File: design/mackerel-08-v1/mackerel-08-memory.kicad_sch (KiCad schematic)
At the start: 8 parts, among them U2 AS6C4008-55PCN, U3 SST39SF040, U4 AS6C4008-55PCN, U5 AS6C4008-55PCN, U6 AS6C4008-55PCN, U7 AS6C4008-55PCN, U8 AS6C4008-55PCN, U9 AS6C4008-55PCN

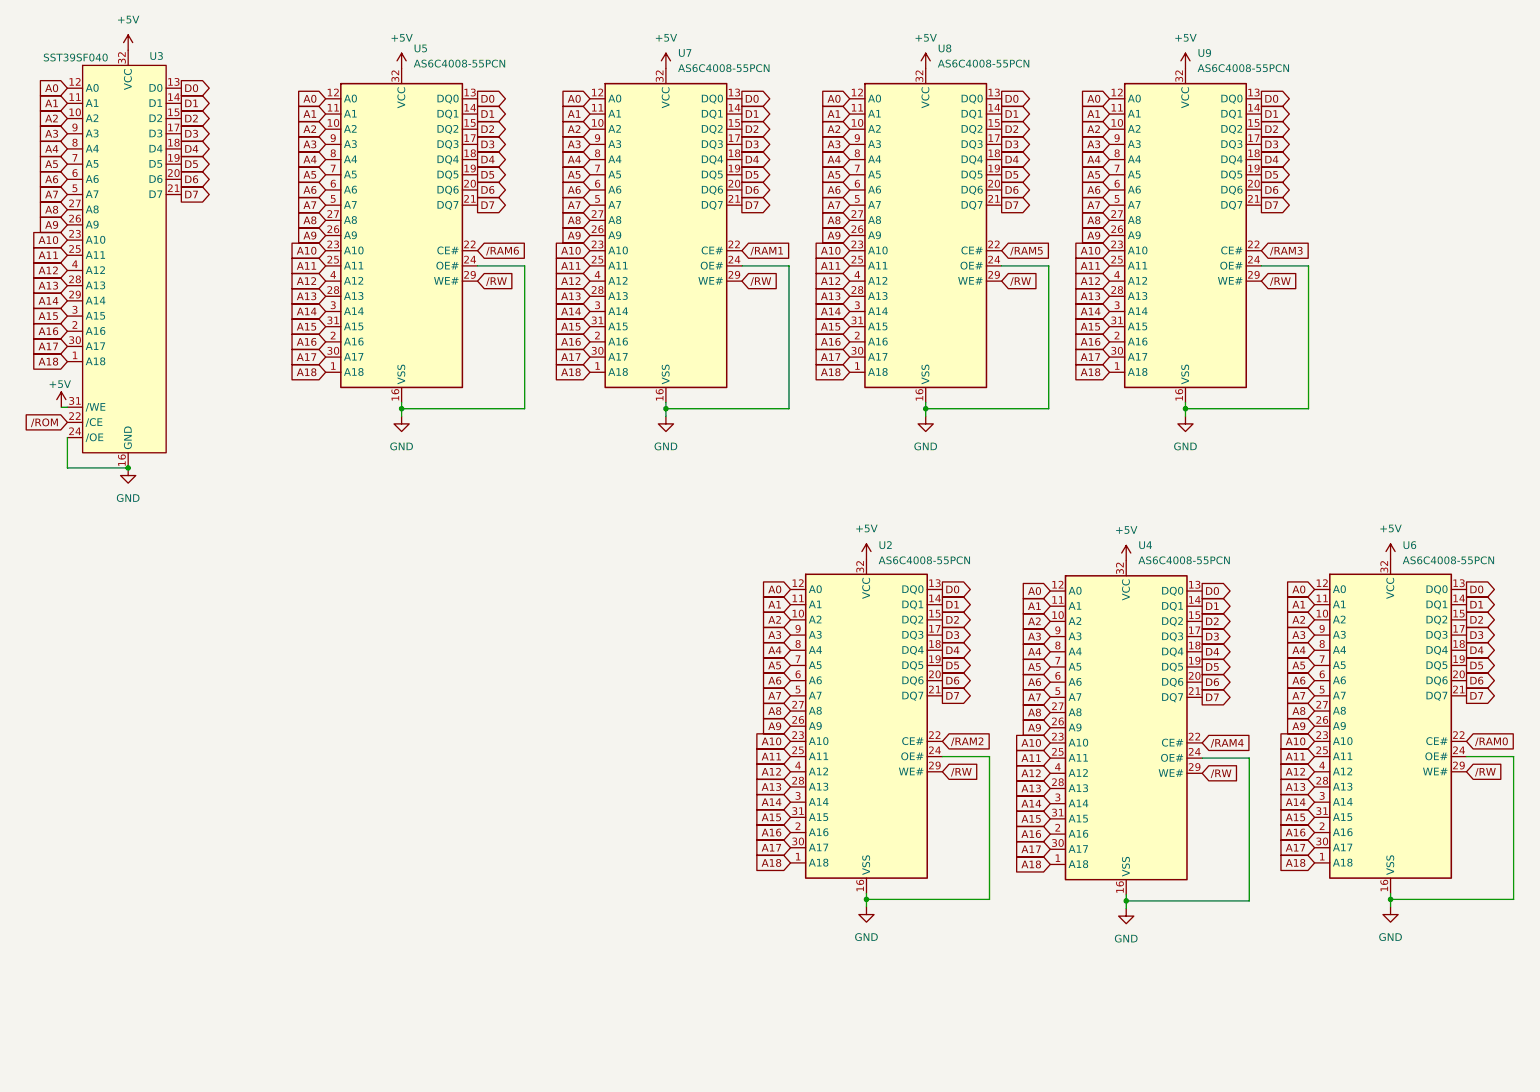
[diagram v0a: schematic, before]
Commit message: Clean up the schematic, ready for final routing
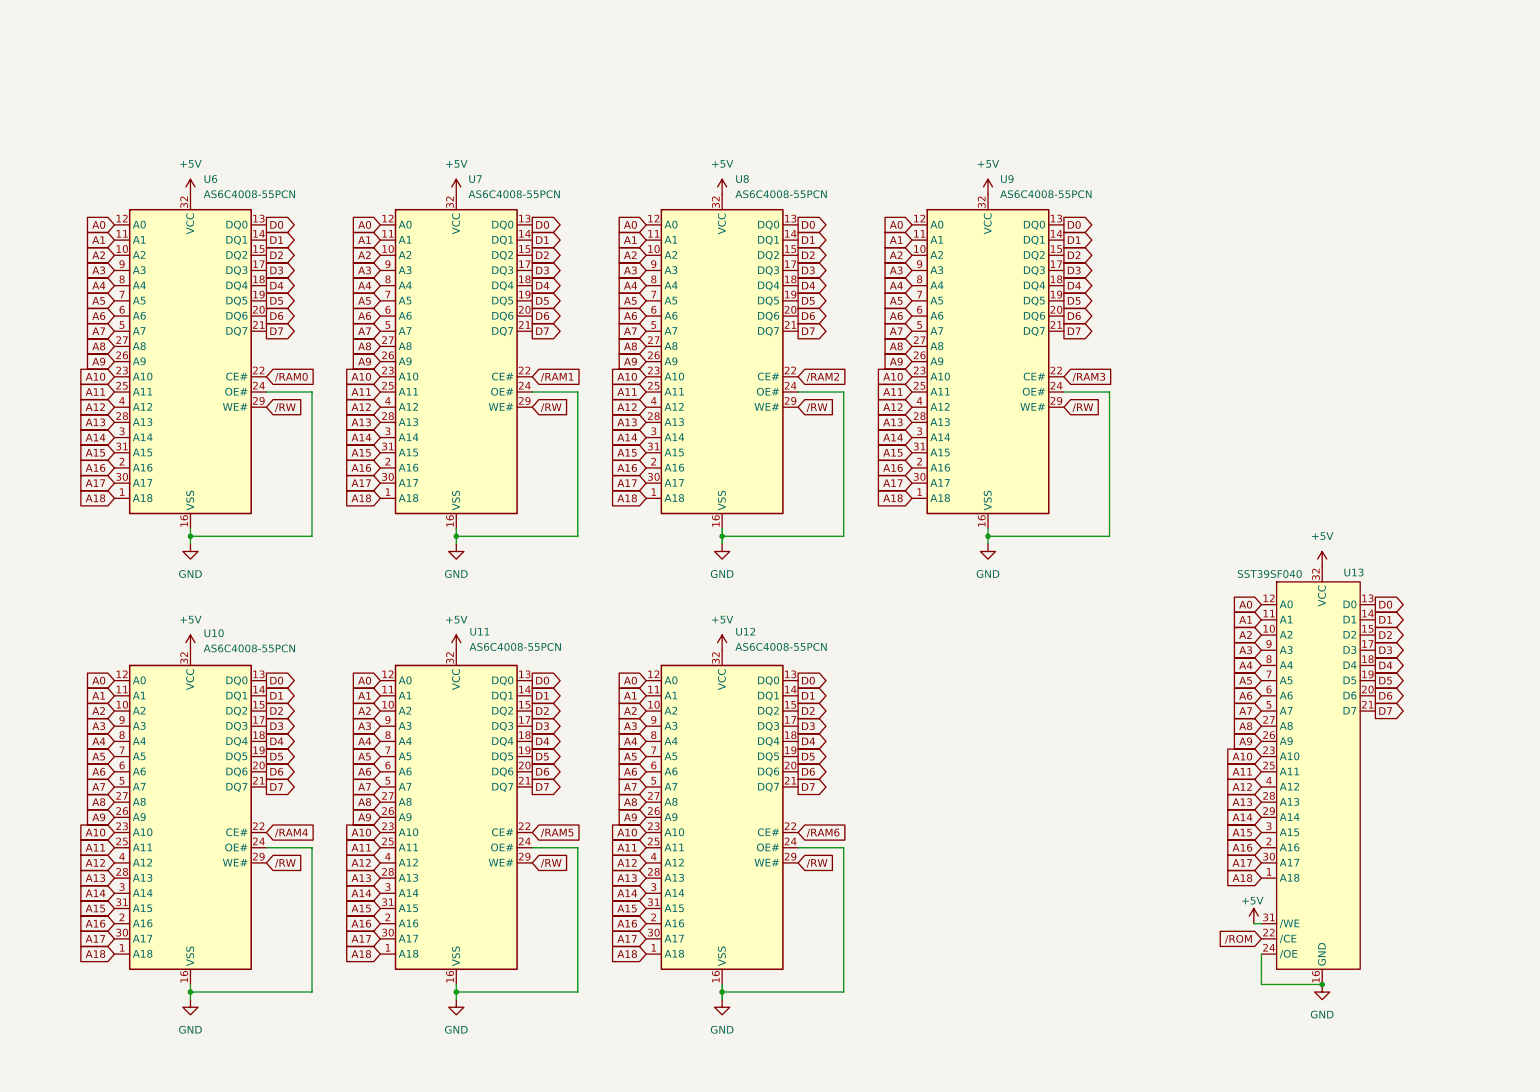
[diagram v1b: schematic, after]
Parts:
- renumbered U4 to U10, U8 to U11, U5 to U12, U3 to U13, U2 to U8
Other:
- company: (none) -> Colin Maykish
- title: (none) -> Mackerel-08 SBC v1
- moved on the sheet: U10, U11, U12, U13, U6, U7, U8, U9

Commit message: Mackerel-08 SVC v1 labeled and ready for final checks
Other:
- note added: "3.5MB SRAM"
- note added: "512KB Flash ROM"
- moved on the sheet: U13
